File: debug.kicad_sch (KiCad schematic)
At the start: 65 parts, among them J701 USB4105-GF-A, J702 2x10 pin IDC, U701 USBLC6-2SC6, U702 FT231XQ-R, U703 TCA9554PW

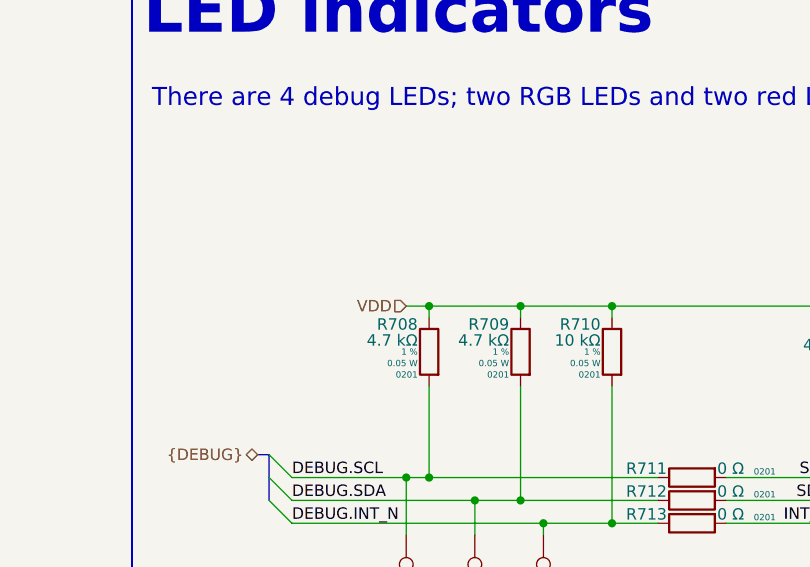
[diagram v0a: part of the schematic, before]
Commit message: Fix power connections
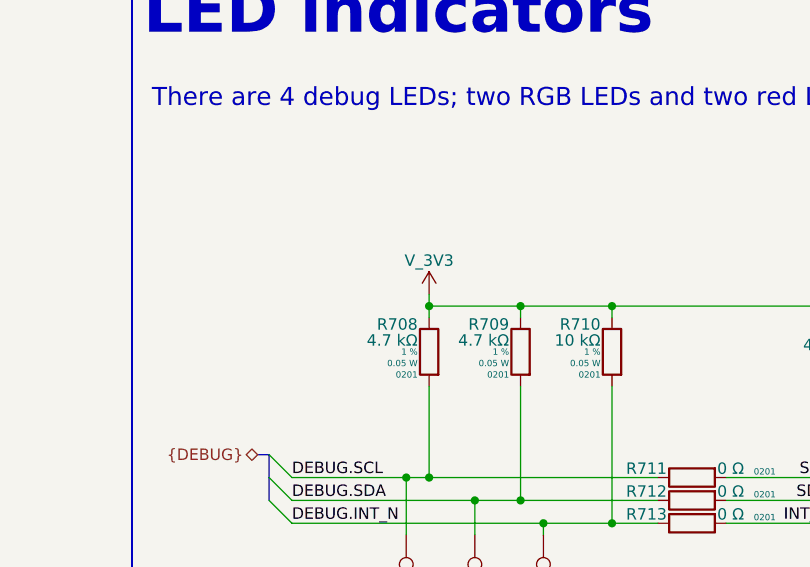
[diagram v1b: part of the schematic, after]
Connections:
- net VDD: no longer C708.1, R708.1, R709.1, R710.1, U703.16 (VDD)
- new net V_3V3: C708.1, R708.1, R709.1, R710.1, U703.16 (VDD)
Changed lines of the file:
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@@
 	)
 	(junction
-		(at 306.07 199.39)
+		(at 185.42 88.9)
 		(diameter 0)
 		(color 0 0 0 0)
 	)
 	(junction
-		(at 152.4 241.3)
+		(at 306.07 199.39)
 		(diameter 0)
 		(color 0 0 0 0)
 	)
 	(junction
-		(at 185.42 88.9)
+		(at 152.4 241.3)
 		(diameter 0)
 		(color 0 0 0 0)
@@
 	(wire
 		(pts
+			(xy 185.42 87.63) (xy 185.42 88.9)
+		)
+		(stroke
+			(width 0)
+			(type default)
+		)
+	)
+	(wire
+		(pts
 			(xy 170.18 113.03) (xy 198.12 113.03)
 		)
@@
 	(wire
 		(pts
-			(xy 182.88 88.9) (xy 185.42 88.9)
-		)
-		(stroke
-			(width 0)
-			(type default)
-		)
-	)
-	(wire
-		(pts
 			(xy 222.25 241.3) (xy 260.35 241.3)
 		)
@@
 		)
 	)
-	(hierarchical_label "VDD"
-		(shape input)
-		(at 182.88 88.9 180)
-		(effects
-			(font
-				(size 1.27 1.27)
-			)
-			(justify right)
-		)
-	)
 	(hierarchical_label "{DEBUG}"
 		(shape bidirectional)
@@
 		(on_board yes)
 		(dnp no)
-		(property "Reference" "#PWR0706"
+		(property "Reference" "#PWR0707"
 			(at 222.25 190.5 0)
 			(effects
@@
 			(project "linux-sbc"
 				(path "/fa11a02f-8043-4153-ab69-88d766503017/5e32b227-0684-45b9-8c92-9550e4036164"
-					(reference "#PWR0706")
+					(reference "#PWR0707")
 					(unit 1)
 				)
@@
 		(dnp no)
 		(fields_autoplaced yes)
-		(property "Reference" "#PWR0708"
+		(property "Reference" "#PWR0709"
 			(at 241.3 139.7 0)
 			(effects
@@
 			(project "linux-sbc"
 				(path "/fa11a02f-8043-4153-ab69-88d766503017/5e32b227-0684-45b9-8c92-9550e4036164"
-					(reference "#PWR0708")
+					(reference "#PWR0709")
 					(unit 1)
 				)
@@
 		(dnp no)
 		(fields_autoplaced yes)
-		(property "Reference" "#PWR0707"
+		(property "Reference" "#PWR0708"
 			(at 234.95 105.41 0)
 			(effects
@@
 			(project "linux-sbc"
 				(path "/fa11a02f-8043-4153-ab69-88d766503017/5e32b227-0684-45b9-8c92-9550e4036164"
-					(reference "#PWR0707")
+					(reference "#PWR0708")
 					(unit 1)
 				)
@@
 	)
 	(symbol
+		(lib_id "power:VCC")
+		(at 185.42 87.63 0)
+		(unit 1)
+		(exclude_from_sim no)
+		(in_bom yes)
+		(on_board yes)
+		(dnp no)
+		(property "Reference" "#PWR0706"
+			(at 185.42 91.44 0)
+			(effects
+				(font
+					(size 1.27 1.27)
+				)
+				(hide yes)
+			)
+		)
+		(property "Value" "V_3V3"
+			(at 185.42 84.582 0)
+			(effects
+				(font
+					(size 1.27 1.27)
+				)
+				(justify bottom)
+			)
+		)
+		(property "Footprint" ""
+			(at 185.42 87.63 0)
+			(effects
+				(font
+					(size 1.27 1.27)
+				)
+				(hide yes)
+			)
+		)
+		(property "Datasheet" ""
+			(at 185.42 87.63 0)
+			(effects
+				(font
+					(size 1.27 1.27)
+				)
+				(hide yes)
+			)
+		)
+		(property "Description" "Power symbol creates a global label with name \"VCC\""
+			(at 185.42 87.63 0)
+			(effects
+				(font
+					(size 1.27 1.27)
+				)
+				(hide yes)
+			)
+		)
+		(pin "1"
+		)
+		(instances
+			(project "linux-sbc"
+				(path "/fa11a02f-8043-4153-ab69-88d766503017/5e32b227-0684-45b9-8c92-9550e4036164"
+					(reference "#PWR0706")
+					(unit 1)
+				)
+			)
+		)
+	)
+	(symbol
 		(lib_name "R_1")
 		(lib_id "Device:R")
@@
 		(on_board yes)
 		(dnp no)
-		(property "Reference" "#PWR0709"
+		(property "Reference" "#PWR0710"
 			(at 266.7 74.93 0)
 			(effects
@@
 			(project "linux-sbc"
 				(path "/fa11a02f-8043-4153-ab69-88d766503017/5e32b227-0684-45b9-8c92-9550e4036164"
-					(reference "#PWR0709")
+					(reference "#PWR0710")
 					(unit 1)
 				)

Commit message: Clean up schematics
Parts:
- removed R725, R726: 0 Ω, Resistor_SMD:R_0805_2012Metric, symbol Device:R
- renumbered D706 to D704, D707 to D705, D704 to D706, D705 to D707, R724 to R719, R727 to R723, R728 to R724, R729 to R725, R730 to R726, R731 to R727, R732 to R728, R733 to R729, R734 to R730, R735 to R731, R719 to R732, R723 to R733
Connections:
- net DEBUG.RX: now also R720.2
- net DEBUG.TX: now also R721.2
- net RGB1_B: now also U703.6 (P2); no longer U703.9 (P4)
- net RGB1_G: now also U703.5 (P1); no longer U703.7 (P3)
- net RGB1_R: now also U703.4 (P0); no longer U703.6 (P2)
- net RGB2_B: now also U703.10 (P5); no longer U703.12 (P7)
- net RGB2_G: now also U703.9 (P4); no longer U703.11 (P6)
- net RGB2_R: now also U703.7 (P3); no longer U703.10 (P5)
- net LED3_K renamed LED3
- net LED3: now also U703.11 (P6); no longer U703.4 (P0)
- net LED4_K renamed LED4
- net LED4: now also U703.12 (P7); no longer U703.5 (P1)
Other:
- note removed: "Combine the 0 Ω resistors in a poka-yoke configuration to easily swap RX/TX."
- moved on the sheet: C702, C703, D704, D705, D706, D707, R706, R707, R719, R723, R724, R725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

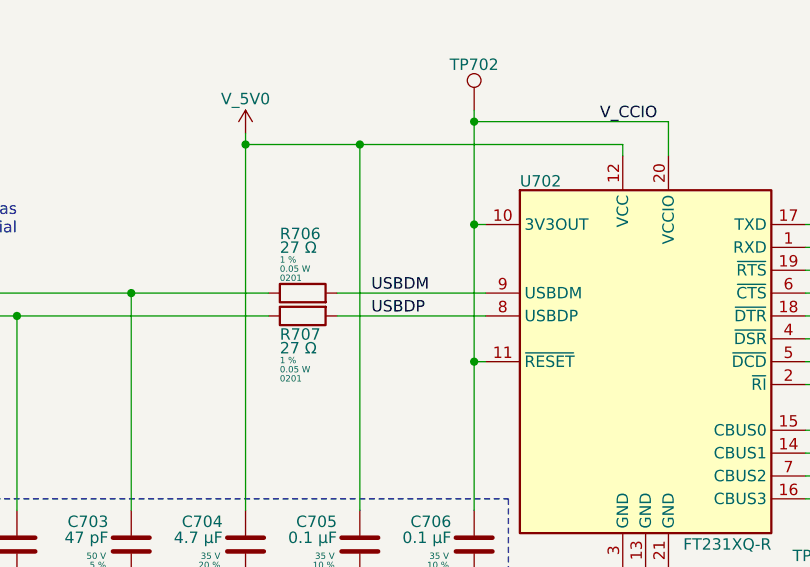
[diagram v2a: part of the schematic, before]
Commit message: Layout the debug section
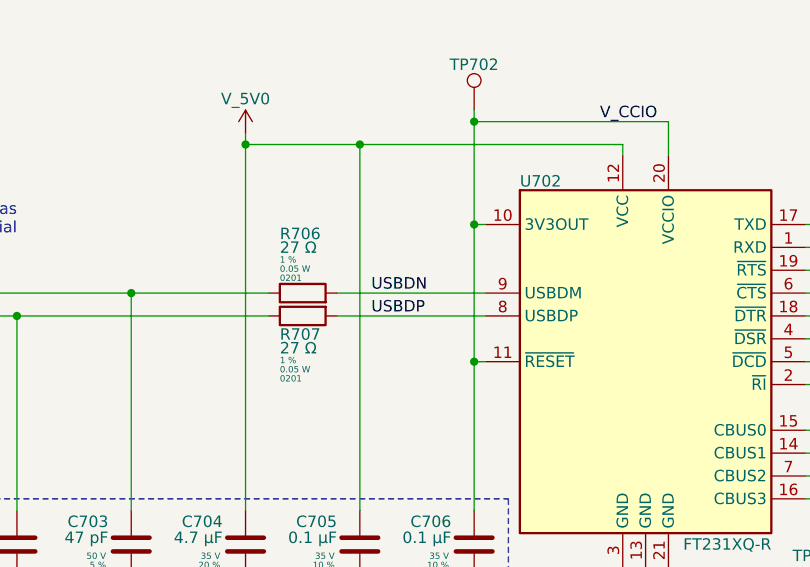
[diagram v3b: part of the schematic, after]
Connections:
- net USBDM renamed USBDN
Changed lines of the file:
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@@
 		)
 	)
-	(label "USBDM"
+	(label "USBDN"
 		(at 153.67 207.01 0)
 		(effects

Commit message: Rework debug with new TVS
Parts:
- removed U701: USBLC6-2SC6, Package_TO_SOT_SMD:SOT-23-6, symbol Power_Protection:USBLC6-2SC6
- added D701: SMAJ5.0A, Diode_SMD:D_SMA, symbol Device:D_Zener
- added D702: DT1240A-08LP3810-7, Package_DFN_QFN:Diodes_UDFN3810-9_TYPE_B, symbol Power_Protection:D3V3X8U9LP3810
- renumbered C708 to C707, C707 to C708, D701 to D703, D702 to D705, D703 to D706, D705 to D707, D706 to D708, D707 to D709, R708 to R706, R709 to R707, R706 to R708, R707 to R709, R719 to R714, R714 to R715, R723 to R716, R724 to R717, R715 to R718, R725 to R719, R726 to R720, R716 to R721, R727 to R722, R728 to R723, R729 to R724, R717 to R725, R718 to R726, R720 to R727, R721 to R728, R722 to R729, TP703 to TP702, TP704 to TP703, TP705 to TP704, TP702 to TP705, U702 to U701, U703 to U702
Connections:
- net D_IN_N is gone; now on net D_N: J701.A7 (D-), J701.B7 (D-)
- net D_IN_P is gone; now on net D_P: J701.A6 (D+), J701.B6 (D+)
- net CHASSIS: now also D701.2 (A), D702.3 (GND)
- net D_N: now also D702.2 (Line-3)
- net D_P: now also D702.1 (Line-1)
- net V_BUS: now also D701.1 (K)
- no-connect marks 6 -> 12
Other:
- moved on the sheet: C702, C703, C704, C705, C706, C708, D703, D705, D706, R708, R709, R715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

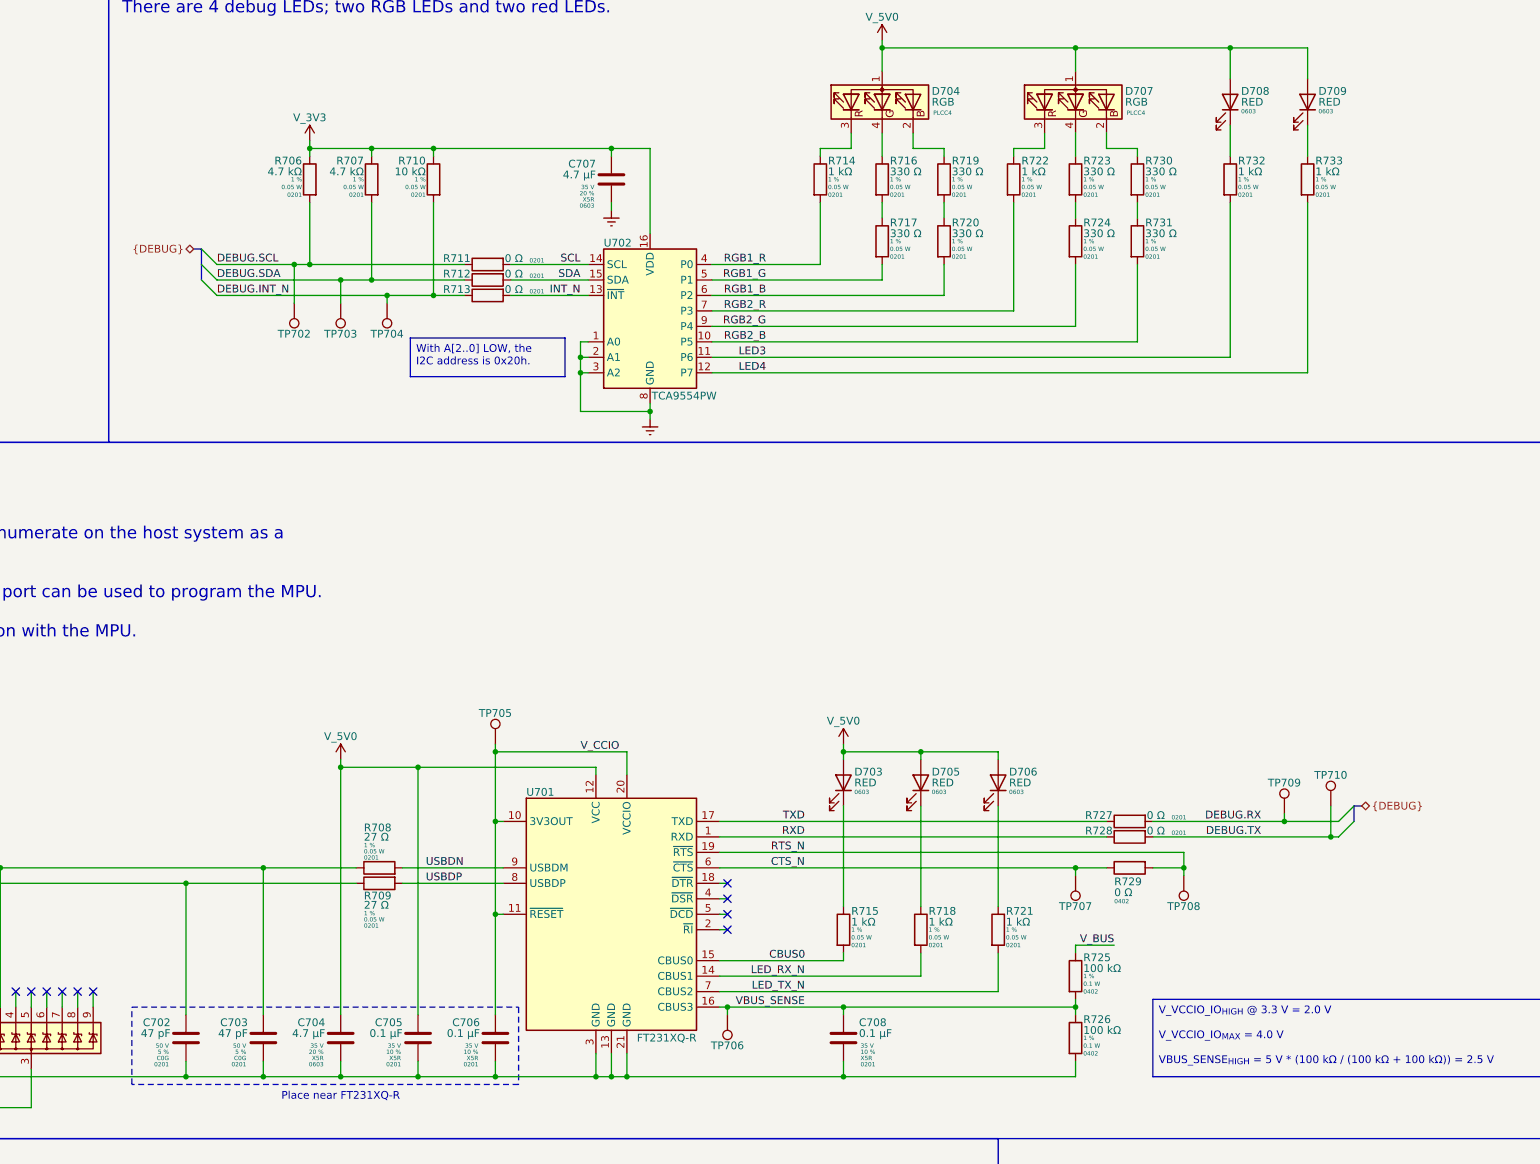
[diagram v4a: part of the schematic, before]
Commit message: Remove redundant test points, fix layouts
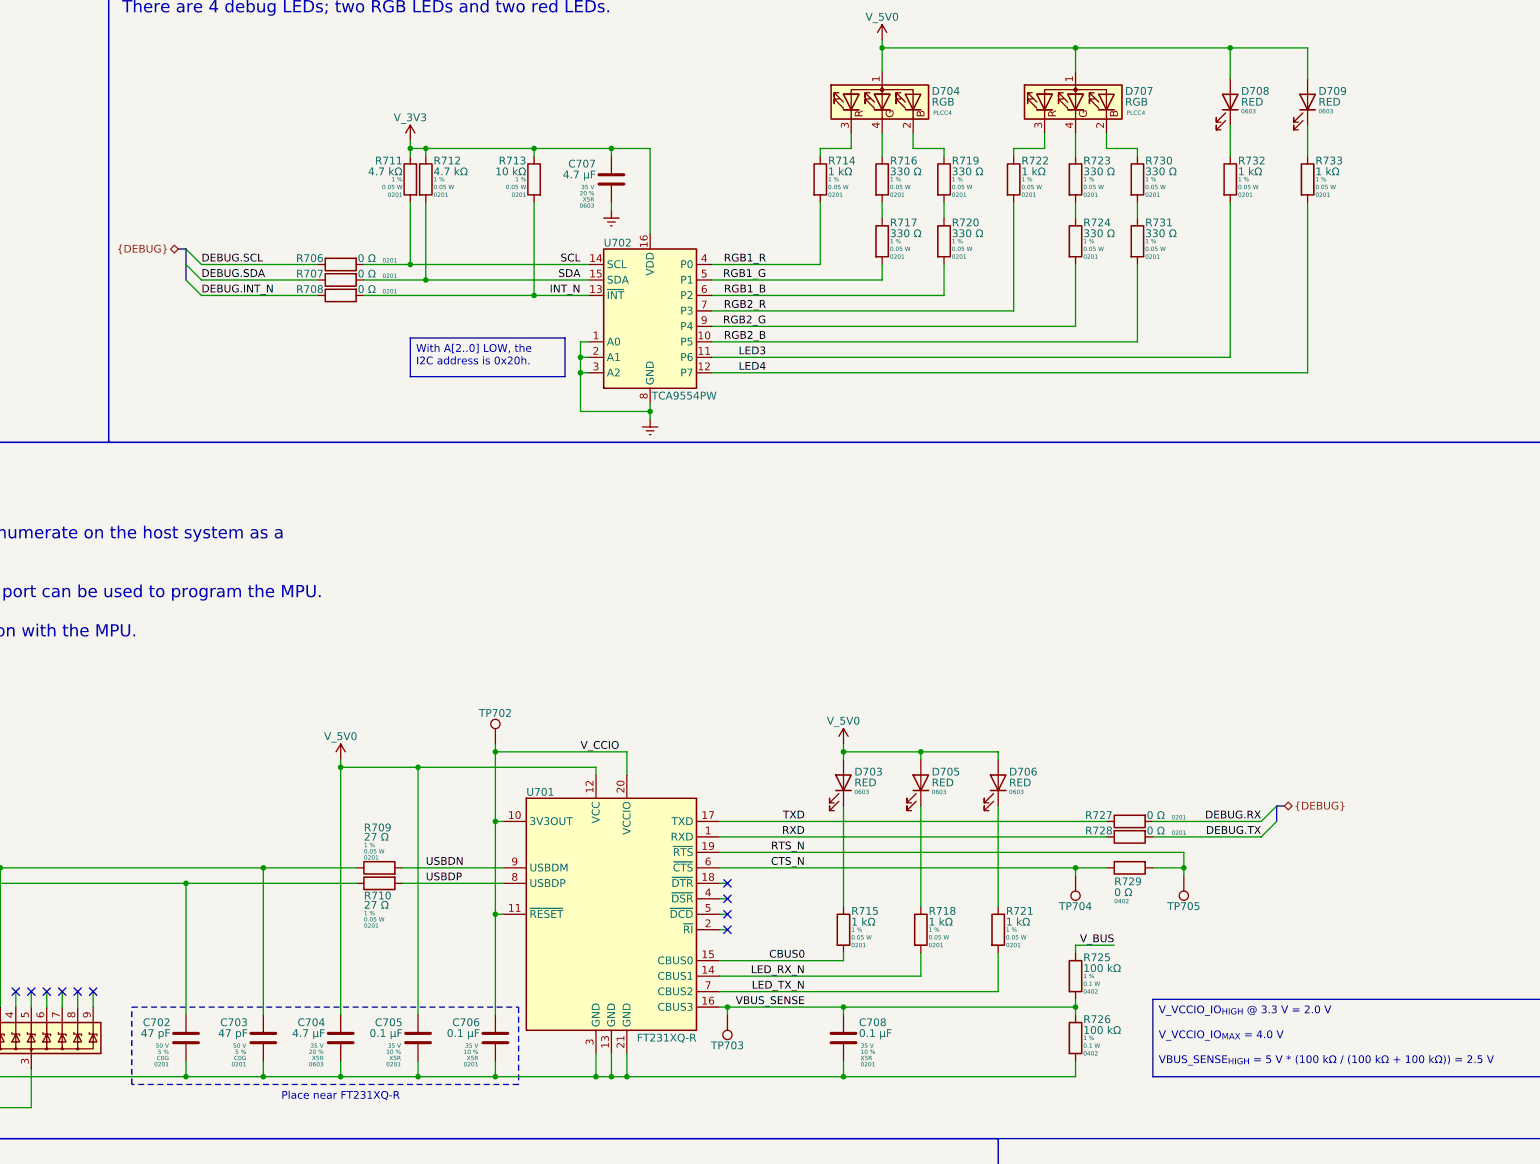
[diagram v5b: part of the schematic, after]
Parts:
- removed TP702, TP703, TP704, TP709, TP710: TestPoint, TestPoint:TestPoint_Pad_D1.0mm, symbol Connector:TestPoint
- renumbered R711 to R706, R712 to R707, R713 to R708, R708 to R709, R709 to R710, R706 to R711, R707 to R712, R710 to R713, TP705 to TP702, TP706 to TP703, TP707 to TP704, TP708 to TP705
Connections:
- net DEBUG.INT_N: no longer R713.2
- net DEBUG.SCL: no longer R711.2
- net DEBUG.SDA: no longer R712.2
- net INT_N: now also R713.2
- net SCL: now also R711.2
- net SDA: now also R712.2
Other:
- moved on the sheet: R706, R707, R708, R711, R712, R713

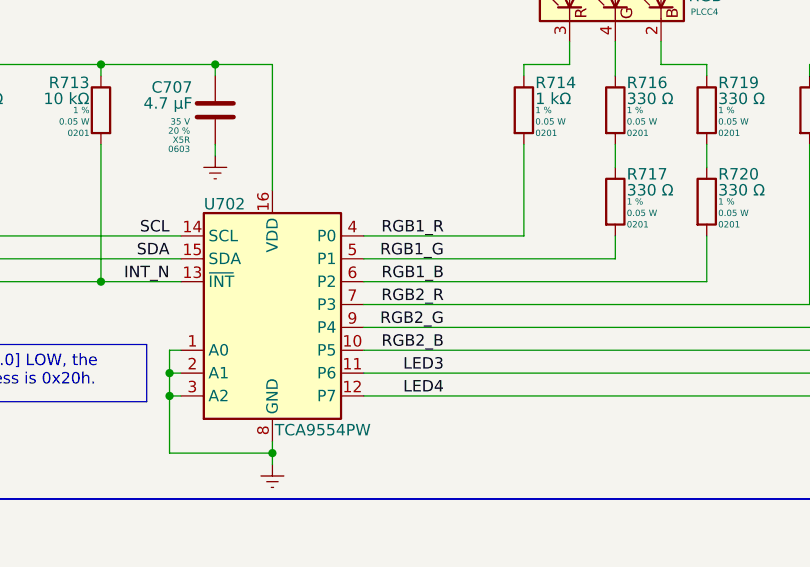
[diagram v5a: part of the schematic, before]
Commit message: Refine and route the debug section
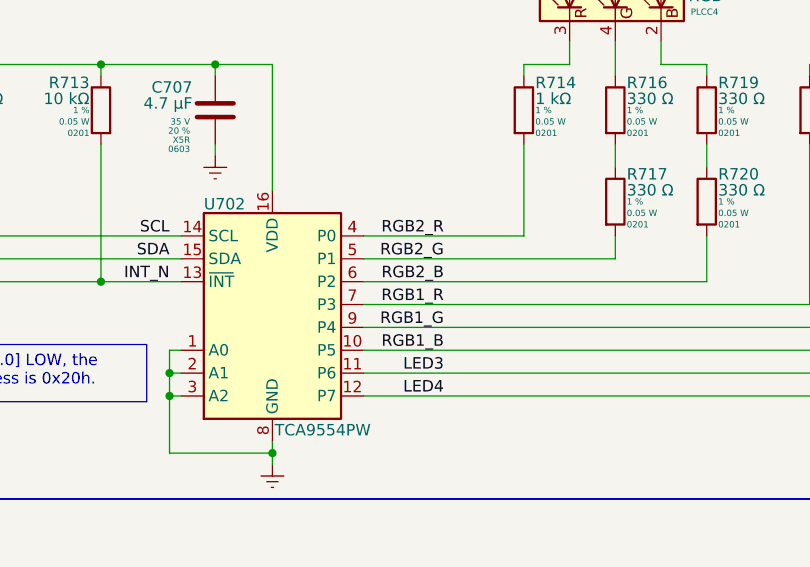
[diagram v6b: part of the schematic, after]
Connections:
- net RGB1_B: now also R731.2, U702.10 (P5); no longer R720.2, U702.6 (P2)
- net RGB1_G: now also R724.2, U702.9 (P4); no longer R717.2, U702.5 (P1)
- net RGB1_R: now also R722.2, U702.7 (P3); no longer R714.2, U702.4 (P0)
- net RGB2_B: now also R720.2, U702.6 (P2); no longer R731.2, U702.10 (P5)
- net RGB2_G: now also R717.2, U702.5 (P1); no longer R724.2, U702.9 (P4)
- net RGB2_R: now also R714.2, U702.4 (P0); no longer R722.2, U702.7 (P3)
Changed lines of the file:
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@@
 	)
 	(label "RGB2_G"
-		(at 260.35 118.11 180)
+		(at 260.35 110.49 180)
 		(effects
 			(font
@@
 	)
 	(label "RGB1_R"
-		(at 260.35 107.95 180)
+		(at 260.35 115.57 180)
 		(effects
 			(font
@@
 	)
 	(label "RGB2_B"
-		(at 260.35 120.65 180)
+		(at 260.35 113.03 180)
 		(effects
 			(font
@@
 	)
 	(label "RGB1_B"
-		(at 260.35 113.03 180)
+		(at 260.35 120.65 180)
 		(effects
 			(font
@@
 	)
 	(label "RGB1_G"
-		(at 260.35 110.49 180)
+		(at 260.35 118.11 180)
 		(effects
 			(font
@@
 	)
 	(label "RGB2_R"
-		(at 260.35 115.57 180)
+		(at 260.35 107.95 180)
 		(effects
 			(font
